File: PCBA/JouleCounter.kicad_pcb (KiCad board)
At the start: 4 copper layers, 42.7 x 59.3 mm, 78 parts, among them IC1001 L7983PU33R, IC901 MP4560DN-LF-Z, J101 JTAG, J501 USB_C_Receptacle, J502 USB_C_Receptacle, J601 USB_C_Receptacle, J901 Conn_02x25_Odd_Even_MountingP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, Q701 2N7002, SW501 SW_DIP_x02, SW801 SW_Push, SW802 SW_Push, SW803 SW_Push, U201 BL706, U301 FUSB302B, U401 FUSB302B, U701 INA226, U702 TC2014-3.3VxCTTR, U901 LP2985-2.8, Y201 40MHz

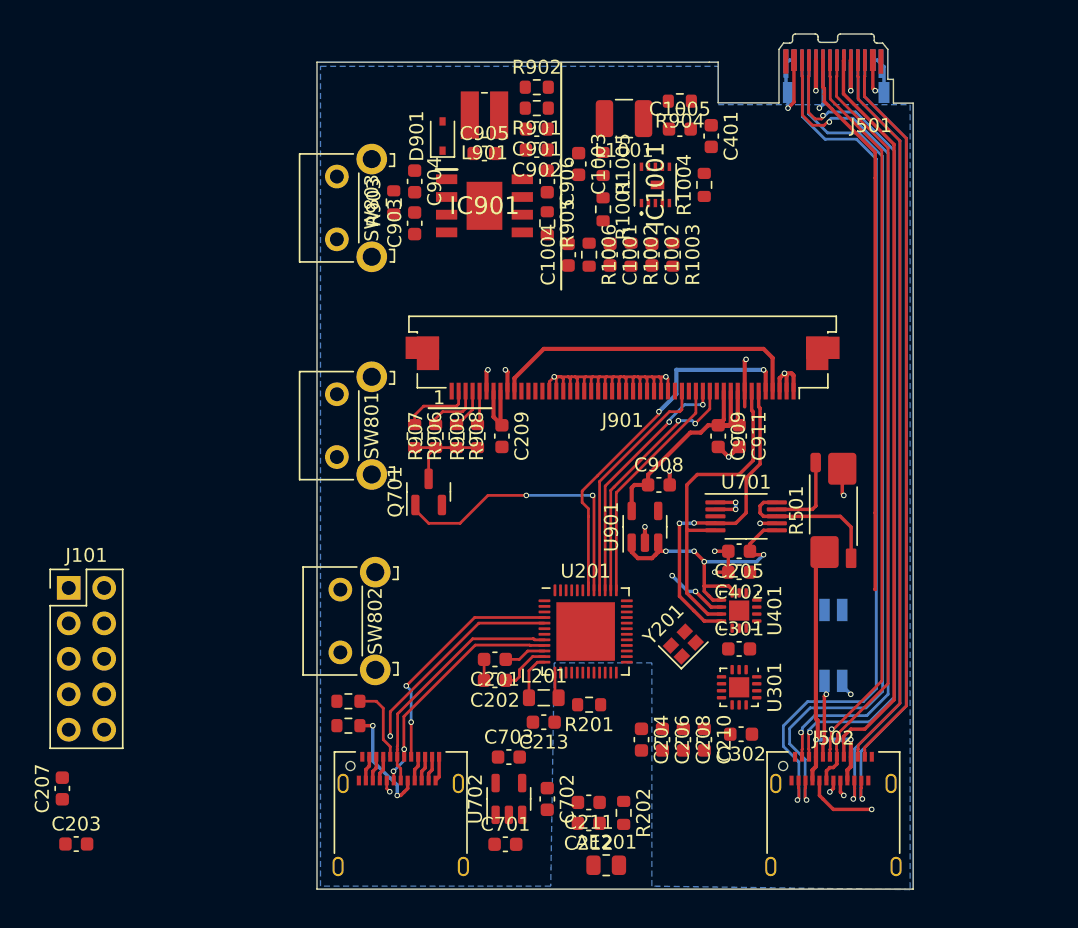
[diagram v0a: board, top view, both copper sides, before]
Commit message: Jtag on usb-c
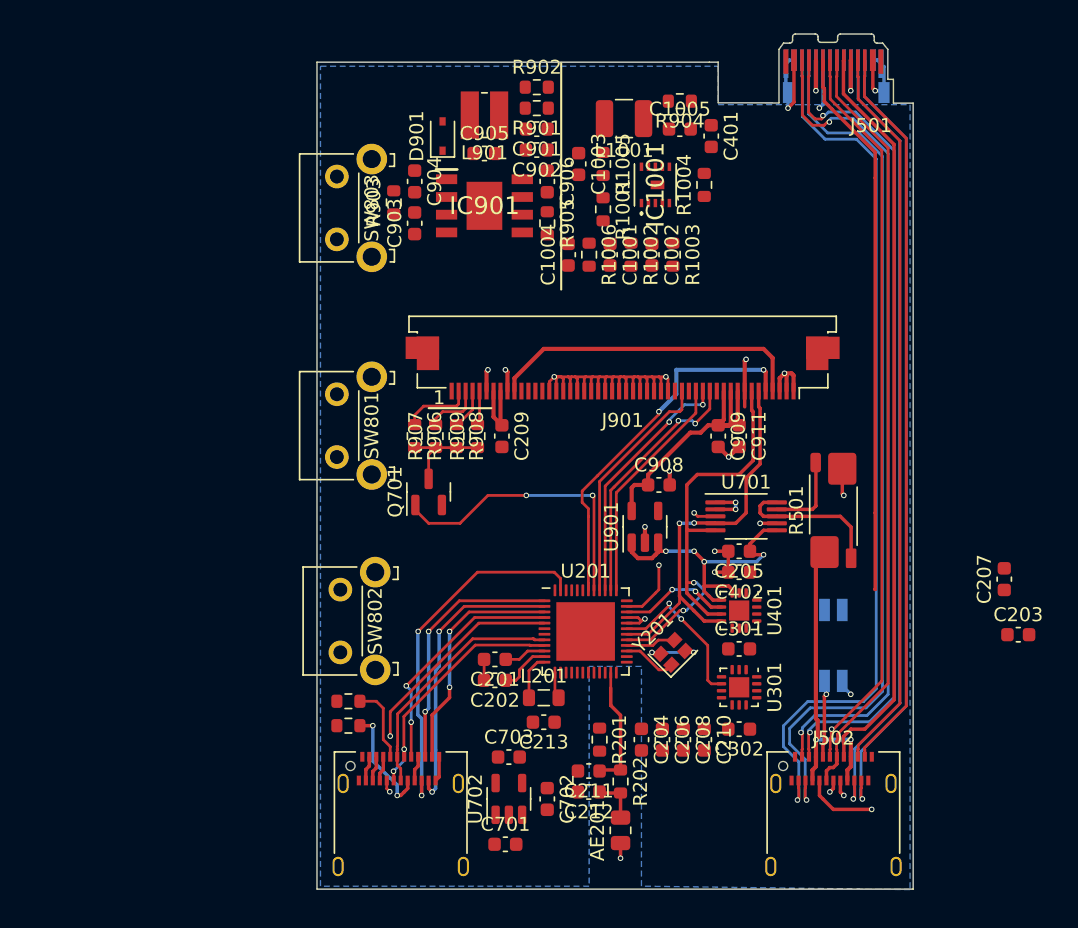
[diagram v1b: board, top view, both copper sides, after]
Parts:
- removed J101: JTAG, Connector_PinHeader_2.54mm:PinHeader_2x05_P2.54mm_Vertical
- moved C203 69.1 mm to (243.8, 101.0)
- moved C207 69.1 mm to (242.8, 97.0)
- moved AE201 2.70 mm to (215.2, 115.0), turned to 90 degrees
- moved R201 2.61 mm to (213.8, 108.5), turned to -90 degrees
- moved R202 2.26 mm to (215.2, 111.5)
- moved C211 2.25 mm to (213.0, 110.8)
- moved C212 2.25 mm to (213.0, 112.2)
- moved Y201 0.96 mm to (219.0, 102.2)
- moved C302 0.39 mm to (223.8, 107.8)
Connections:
- J601 pad A10: /Spare GPIO 0 -> /JTAG TMS
- J601 pad A11: /Spare GPIO 1 -> /JTAG TCK
- J601 pad A2: /SCL -> /SCL1
- J601 pad A3: /SDA -> /SDA1
- J601 pad B10: /SDA -> /SDA1
- J601 pad B11: /SCL -> /SCL1
- J601 pad B2: /Spare GPIO 1 -> /JTAG TDI
- J601 pad B3: /Spare GPIO 0 -> /JTAG TDO
- U201 pad 31: /Main MCU/GPIO 16 -> /~{FUSB IRQ1}
- U201 pad 34: /~{ADC IRQ} -> /~{FUSB IRQ0}
- U201 pad 35: /Spare GPIO 0 -> /~{ADC IRQ}
- U201 pad 46: /Spare GPIO 1 -> /Main MCU/GPIO 30
- U201 pad 6: /~{FUSB IRQ0} -> /Main MCU/GPIO 5
- U201 pad 7: /~{FUSB IRQ1} -> /Main MCU/GPIO 6
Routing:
- net /JTAG TDO: track 0.00 -> 25.9 mm, vias 0 -> 2
- net /JTAG TDI: track 0.00 -> 20.9 mm, vias 0 -> 2
- net /JTAG TMS: track 0.00 -> 18.3 mm, vias 0 -> 2
- net /JTAG TCK: track 0.00 -> 16.9 mm, vias 0 -> 2
- net /~{ADC IRQ}: track 0.00 -> 12.0 mm, vias 0 -> 2
- net /~{FUSB IRQ1}: track 0.00 -> 11.6 mm, vias 0 -> 2
- net /Main MCU/RF: track 0.00 -> 9.20 mm
- net /SCL: track 25.2 -> 32.0 mm, vias 0 -> 2
- net GND: track 68.7 -> 74.1 mm, vias 16 -> 19
- net Net-(U201-Pad27): track 0.00 -> 3.90 mm
- net Net-(U201-Pad28): track 0.00 -> 3.57 mm
- net /~{FUSB IRQ0}: track 4.47 -> 7.97 mm
- net /SDA: track 25.1 -> 28.4 mm
- net /Main MCU/ANT: track 0.00 -> 3.29 mm
- net /SENSE_USB_D-: track 55.2 -> 57.7 mm, vias 0 -> 1
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
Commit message: Finish routing
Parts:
- added R101: 10k, Resistor_SMD:R_0603_1608Metric, F.Cu at (208.2, 86.8)
- moved C207 35.5 mm to (207.2, 97.5), turned to 180 degrees
- moved C401 22.4 mm to (214.0, 86.2)
- moved C203 21.2 mm to (226.2, 89.0), turned to 90 degrees
- moved C210 4.16 mm to (219.0, 105.0), turned to 0 degrees
- moved C204 2.55 mm to (216.2, 106.0)
- moved C206 1.35 mm to (217.8, 107.2)
- moved C208 1.35 mm to (219.2, 107.2)
- moved C213 1.25 mm to (210.5, 106.2), turned to -90 degrees
- moved L201 1.25 mm to (208.8, 106.2), turned to -90 degrees
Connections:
- J501 pad A4: /Measurement ports/VBUS2 -> /VBus
- J501 pad A9: /Measurement ports/VBUS2 -> /VBus
- J501 pad B4: /Measurement ports/VBUS2 -> /VBus
- J501 pad B9: /Measurement ports/VBUS2 -> /VBus
- J502 pad A4: /VBus -> /Measurement ports/VBUS2
- J502 pad A9: /VBus -> /Measurement ports/VBUS2
- J502 pad B4: /VBus -> /Measurement ports/VBUS2
- J502 pad B9: /VBus -> /Measurement ports/VBUS2
- J901 pad 4: /~{Reset} -> /UI/~{LCD Reset}
- J901 pad 41: /~{Reset} -> /UI/~{LCD Reset}
- J901 pad MP: unconnected-(J901-PadMP) -> GND
- R501 pad 1: /VBus -> /Measurement ports/VBUS2
- R501 pad 4: /Measurement ports/VBUS2 -> /VBus
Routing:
- net /5V_USB: track 3.61 -> 133.8 mm, vias 0 -> 8
- net VDD: track 27.1 -> 134.8 mm, vias 4 -> 20
- net GND: track 74.1 -> 172.3 mm, vias 19 -> 66
- net /CC2: track 0.00 -> 54.6 mm, vias 0 -> 3
- net /Power/EN: track 0.00 -> 40.6 mm, vias 0 -> 4
- net /Button A: track 0.00 -> 38.6 mm
- net /SCL1: track 1.80 -> 39.1 mm, vias 0 -> 3
- net /SDA1: track 1.80 -> 36.7 mm, vias 0 -> 3
- net /SENSE_USB_D+: track 58.7 -> 90.8 mm, vias 2 -> 4
- net /VBus: track 22.4 -> 53.7 mm, vias 2 -> 23
- net /SENSE_USB_D-: track 57.7 -> 86.4 mm, vias 1 -> 3
- net /UI/~{LCD Reset}: track 0.00 -> 25.6 mm
- net /BootMode: track 0.00 -> 24.7 mm
- net Net-(IC901-Pad4): track 0.00 -> 21.9 mm, vias 0 -> 2
- net /Button C: track 0.00 -> 20.7 mm
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- added copper zone on F.Cu, net /Measurement ports/VBUS2
- added copper zone on In1.Cu, net /Measurement ports/VBUS2
- added copper zone on F.Cu, net /VBus
- added copper zone on In1.Cu, net /VBus
- added copper zone on In2.Cu, net /VBus
- added copper zone on F.Cu, net GND
- added copper zone on In1.Cu, net GND
- added copper zone on In2.Cu, net GND
- added copper zone on In1.Cu, net VDD
- added copper zone on In2.Cu, net VDD
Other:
- board text added: "~Potato~"

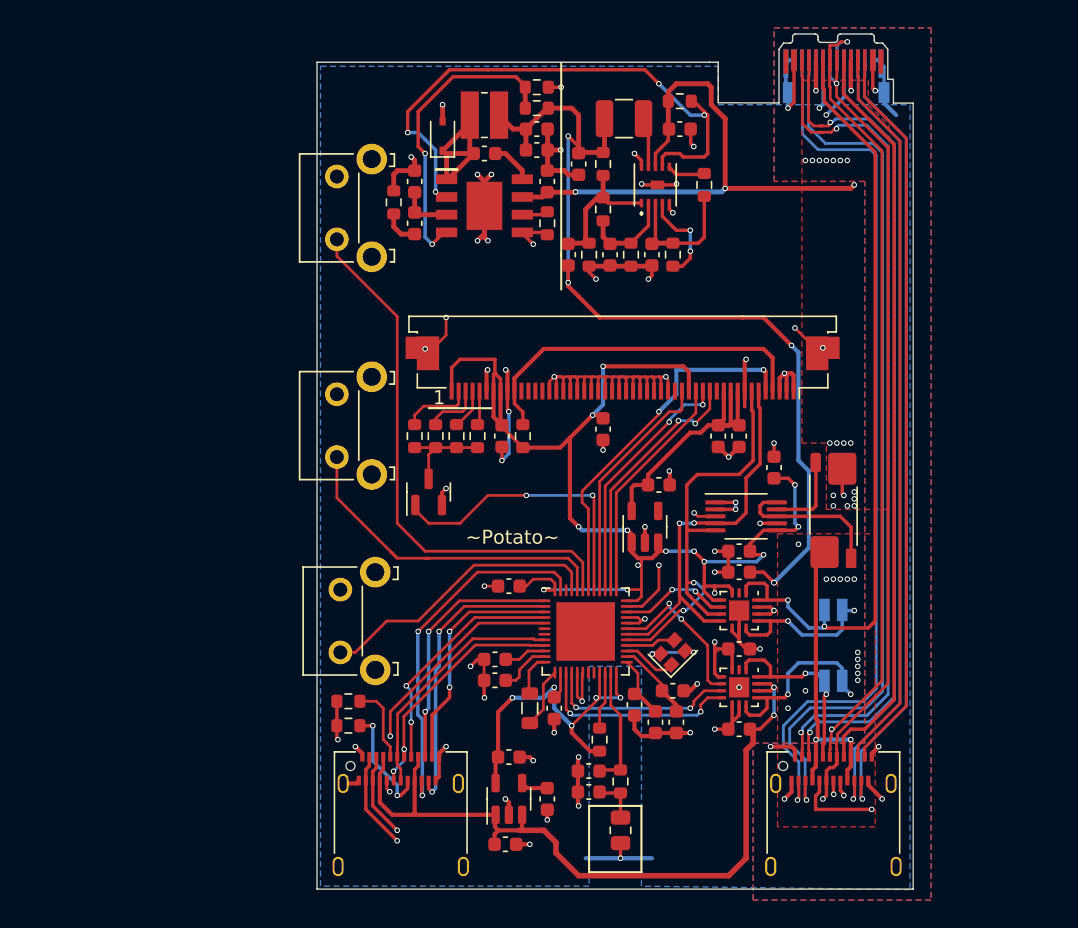
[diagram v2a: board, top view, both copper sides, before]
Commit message: Fix up via hole size
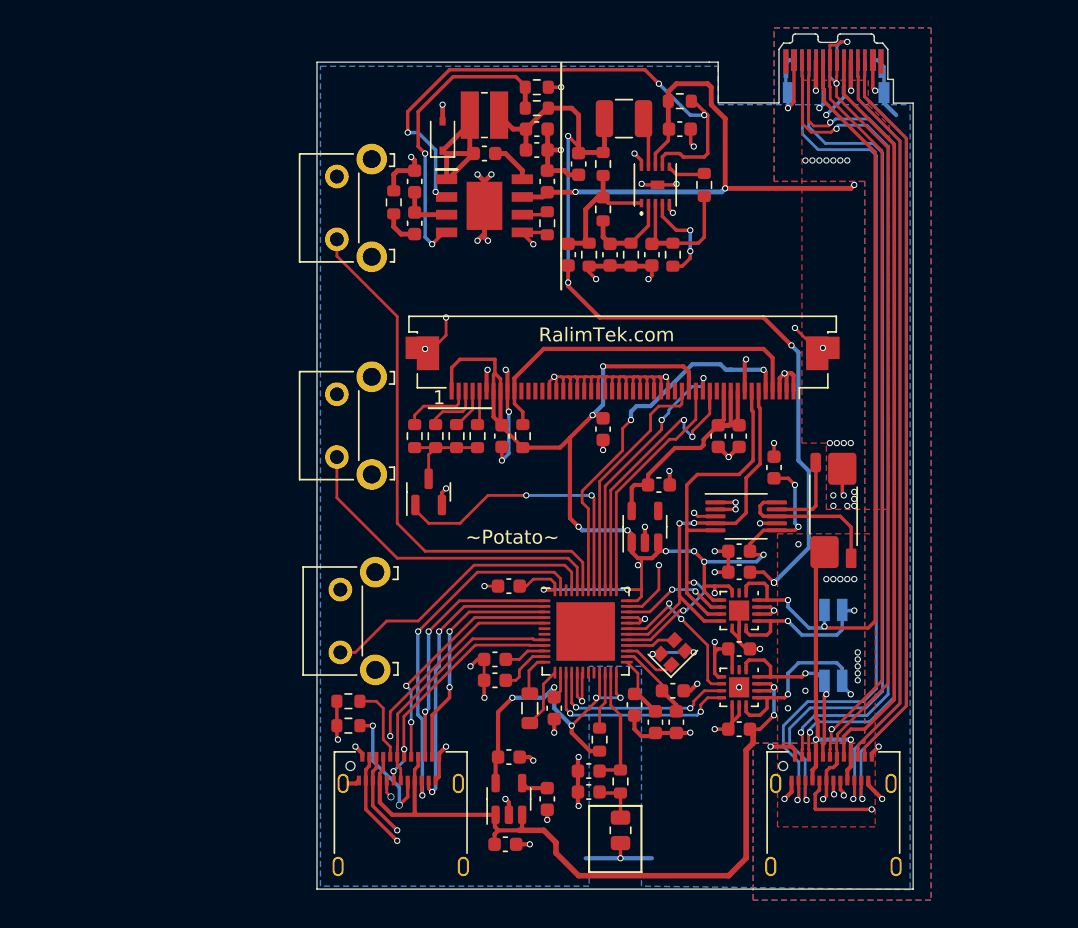
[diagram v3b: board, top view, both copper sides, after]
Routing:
- net GND: track 172.3 -> 165.4 mm
- net /LCD CS: track 18.2 -> 21.2 mm
- net Net-(J601-PadB5): track 8.18 -> 10.0 mm
- net VDD: track 134.8 -> 133.2 mm
- net /LCD SCK: track 17.9 -> 19.4 mm
- net /Uart Rx: track 20.5 -> 21.9 mm
- net Net-(C905-Pad1): track 13.4 -> 12.4 mm
- net /Measurement ports/VBUS2: track 22.4 -> 21.5 mm
- net /BootMode: track 24.7 -> 23.9 mm
- net /5V_USB: track 133.8 -> 133.1 mm
- net /~{TOUCH_IRQ}: track 27.5 -> 28.2 mm
- net Net-(C204-Pad1): track 4.73 -> 4.12 mm
- net /Power/EN: track 40.6 -> 40.0 mm
- net /USB D-: track 18.2 -> 17.7 mm
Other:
- board text added: "RalimTek.com"
